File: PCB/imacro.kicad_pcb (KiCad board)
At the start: 2 copper layers, 55.1 x 73.6 mm, 29 parts, among them SW0:0 Choc, SW0:1 Choc, SW0:2 Choc, SW1 TOGGLE, SW1:0 Choc, SW1:1 Choc, SW1:2 Choc, SW2:0 Choc, SW2:1 Choc, SW2:2 Choc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

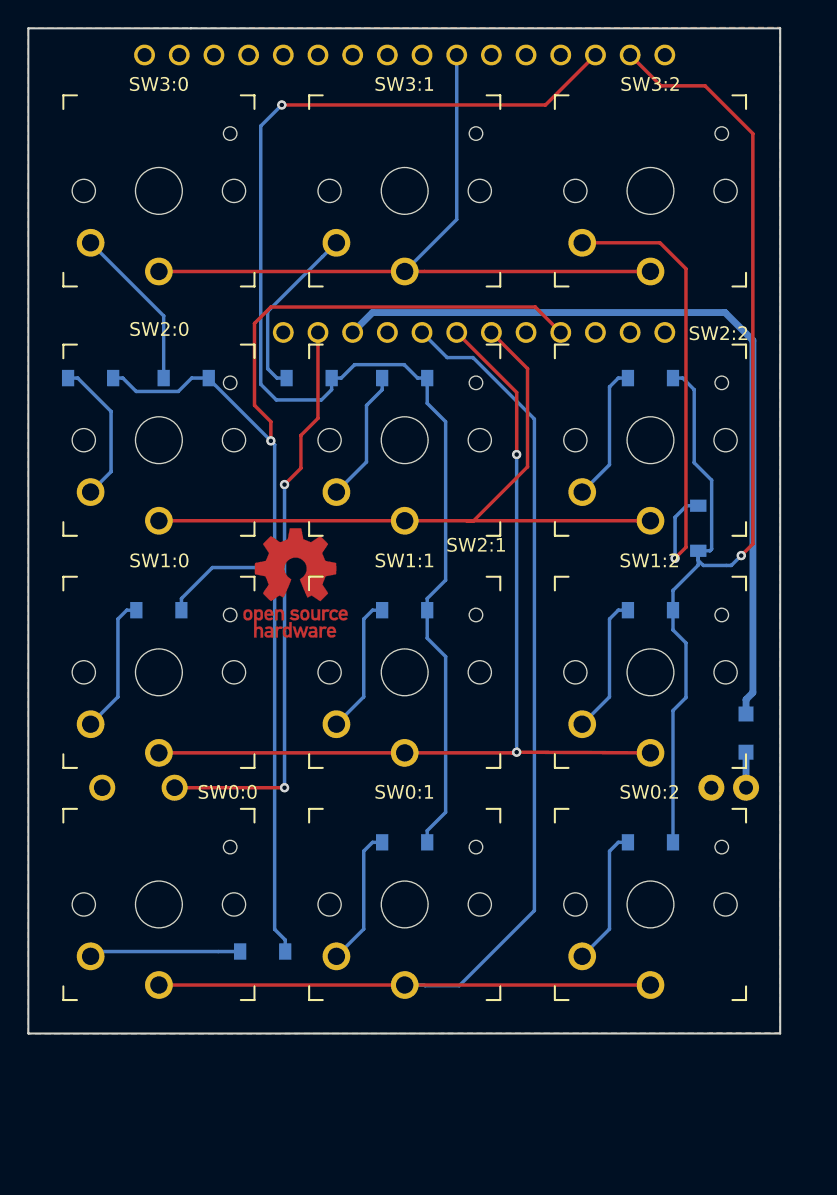
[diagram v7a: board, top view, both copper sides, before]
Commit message: Stitch ground fills to reduce ground loops
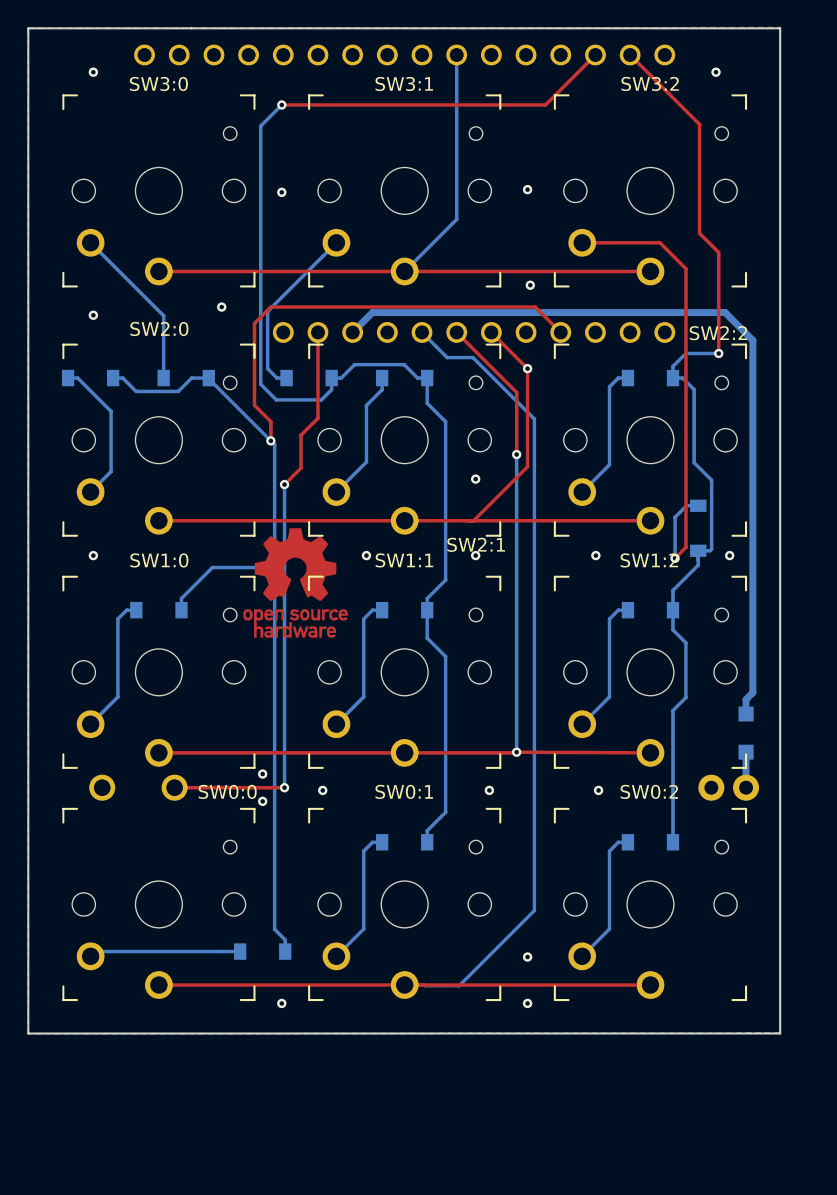
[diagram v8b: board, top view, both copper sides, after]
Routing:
- net /COL2: track 85.1 -> 68.0 mm
- net GND: vias 0 -> 21
- net /ROW2: vias 0 -> 1
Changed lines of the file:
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@@
     (thickness 1.6)
     (drawings 9)
-    (tracks 174)
+    (tracks 196)
     (zones 0)
     (modules 29)
@@
   (segment (start 118.65 102.35) (end 119.6 101.4) (width 0.254) (layer B.Cu) (net 5))
   (segment (start 118.65 112) (end 118.65 102.35) (width 0.254) (layer B.Cu) (net 5))
-  (segment (start 120.869901 91.723901) (end 122.547473 91.723901) (width 0.254) (layer B.Cu) (net 5))
-  (segment (start 120.5 91.354) (end 120.869901 91.723901) (width 0.254) (layer B.Cu) (net 5))
   (segment (start 120.5 90.65) (end 120.5 91.354) (width 0.254) (layer B.Cu) (net 5))
-  (segment (start 122.547473 91.723901) (end 122.876099 91.723901) (width 0.254) (layer B.Cu) (net 5))
-  (via (at 123.6491 91) (size 0.6858) (drill 0.3302) (layers F.Cu B.Cu) (net 5))
-  (segment (start 122.925199 91.723901) (end 123.6491 91) (width 0.254) (layer B.Cu) (net 5))
-  (segment (start 122.876099 91.723901) (end 122.925199 91.723901) (width 0.254) (layer B.Cu) (net 5))
-  (segment (start 124.5 90.1491) (end 123.6491 91) (width 0.254) (layer F.Cu) (net 5))
-  (segment (start 124.5 60.1) (end 124.5 90.1491) (width 0.254) (layer F.Cu) (net 5))
-  (segment (start 121 56.6) (end 124.5 60.1) (width 0.254) (layer F.Cu) (net 5))
-  (segment (start 117.77 56.6) (end 121 56.6) (width 0.254) (layer F.Cu) (net 5))
   (segment (start 115.51 54.34) (end 117.77 56.6) (width 0.254) (layer F.Cu) (net 5))
   (segment (start 121.481001 90.522999) (end 121.481001 85.481001) (width 0.254) (layer B.Cu) (net 5))
@@
   (segment (start 120.2 78.846) (end 119.354 78) (width 0.254) (layer B.Cu) (net 5))
   (segment (start 120.2 84.2) (end 120.2 78.846) (width 0.254) (layer B.Cu) (net 5))
+  (segment (start 118.65 77.146) (end 119.596 76.2) (width 0.254) (layer B.Cu) (net 5))
+  (segment (start 119.596 76.2) (end 120.6 76.2) (width 0.254) (layer B.Cu) (net 5))
+  (segment (start 118.65 78) (end 118.65 77.146) (width 0.254) (layer B.Cu) (net 5))
+  (segment (start 120.6 59.43) (end 117.77 56.6) (width 0.254) (layer F.Cu) (net 5))
+  (via (at 122 76.2) (size 0.6858) (drill 0.3302) (layers F.Cu B.Cu) (net 5))
+  (segment (start 120.6 76.2) (end 122 76.2) (width 0.254) (layer B.Cu) (net 5))
+  (segment (start 122 76.2) (end 122 68.8) (width 0.254) (layer F.Cu) (net 5))
+  (segment (start 120.6 67.4) (end 120.6 59.43) (width 0.254) (layer F.Cu) (net 5))
+  (segment (start 122 68.8) (end 120.6 67.4) (width 0.254) (layer F.Cu) (net 5))
   (segment (start 114.646 112) (end 114 112.646) (width 0.254) (layer B.Cu) (net 6))
   (segment (start 115.35 112) (end 114.646 112) (width 0.254) (layer B.Cu) (net 6))
@@
   (segment (start 119.6 90.4) (end 119.6 70) (width 0.254) (layer F.Cu) (net 17))
   (segment (start 118.8 91.2) (end 119.6 90.4) (width 0.254) (layer F.Cu) (net 17))
+  (via (at 93 108.2) (size 0.6858) (drill 0.3302) (layers F.Cu B.Cu) (net 18))
+  (via (at 105.2 108.2) (size 0.6858) (drill 0.3302) (layers F.Cu B.Cu) (net 18))
+  (via (at 113.2 108.2) (size 0.6858) (drill 0.3302) (layers F.Cu B.Cu) (net 18))
+  (via (at 88.6 109) (size 0.6858) (drill 0.3302) (layers F.Cu B.Cu) (net 18))
+  (via (at 88.6 107) (size 0.6858) (drill 0.3302) (layers F.Cu B.Cu) (net 18))
+  (via (at 113 91) (size 0.6858) (drill 0.3302) (layers F.Cu B.Cu) (net 18))
+  (via (at 104.2 91) (size 0.6858) (drill 0.3302) (layers F.Cu B.Cu) (net 18))
+  (via (at 96.2 91) (size 0.6858) (drill 0.3302) (layers F.Cu B.Cu) (net 18))
+  (via (at 76.2 91) (size 0.6858) (drill 0.3302) (layers F.Cu B.Cu) (net 18))
+  (via (at 76.2 73.4) (size 0.6858) (drill 0.3302) (layers F.Cu B.Cu) (net 18))
+  (via (at 121.8 55.6) (size 0.6858) (drill 0.3302) (layers F.Cu B.Cu) (net 18))
+  (via (at 76.2 55.6) (size 0.6858) (drill 0.3302) (layers F.Cu B.Cu) (net 18))
+  (via (at 108 64.2) (size 0.6858) (drill 0.3302) (layers F.Cu B.Cu) (net 18))
+  (via (at 90 64.4) (size 0.6858) (drill 0.3302) (layers F.Cu B.Cu) (net 18))
+  (via (at 90 123.8) (size 0.6858) (drill 0.3302) (layers F.Cu B.Cu) (net 18))
+  (via (at 108 123.8) (size 0.6858) (drill 0.3302) (layers F.Cu B.Cu) (net 18))
+  (via (at 108 120.4) (size 0.6858) (drill 0.3302) (layers F.Cu B.Cu) (net 18))
+  (via (at 122.8 91) (size 0.6858) (drill 0.3302) (layers F.Cu B.Cu) (net 18))
+  (via (at 104.2 85.4) (size 0.6858) (drill 0.3302) (layers F.Cu B.Cu) (net 18))
+  (via (at 85.6 72.8) (size 0.6858) (drill 0.3302) (layers F.Cu B.Cu) (net 18))
+  (via (at 108.2 71.2) (size 0.6858) (drill 0.3302) (layers F.Cu B.Cu) (net 18))
   (segment (start 117 122.45) (end 99 122.45) (width 0.254) (layer F.Cu) (net 19))
   (segment (start 99 122.45) (end 81 122.45) (width 0.254) (layer F.Cu) (net 19))
@@
   (segment (start 108 77.31) (end 108 84.5) (width 0.254) (layer F.Cu) (net 21))
   (segment (start 105.35 74.66) (end 108 77.31) (width 0.254) (layer F.Cu) (net 21))
+  (segment (start 108 77.31) (end 108 77.31) (width 0.254) (layer F.Cu) (net 21))
+  (via (at 108 77.31) (size 0.6858) (drill 0.3302) (layers F.Cu B.Cu) (net 21))
   (segment (start 100.43684 70.19375) (end 117 70.19375) (width 0.254) (layer F.Cu) (net 22))
   (segment (start 99 70.19375) (end 100.43684 70.19375) (width 0.254) (layer F.Cu) (net 22))
